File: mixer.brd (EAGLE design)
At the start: 23 x 40 mm, 21 parts, among them U2 SA602AD8-SOIC

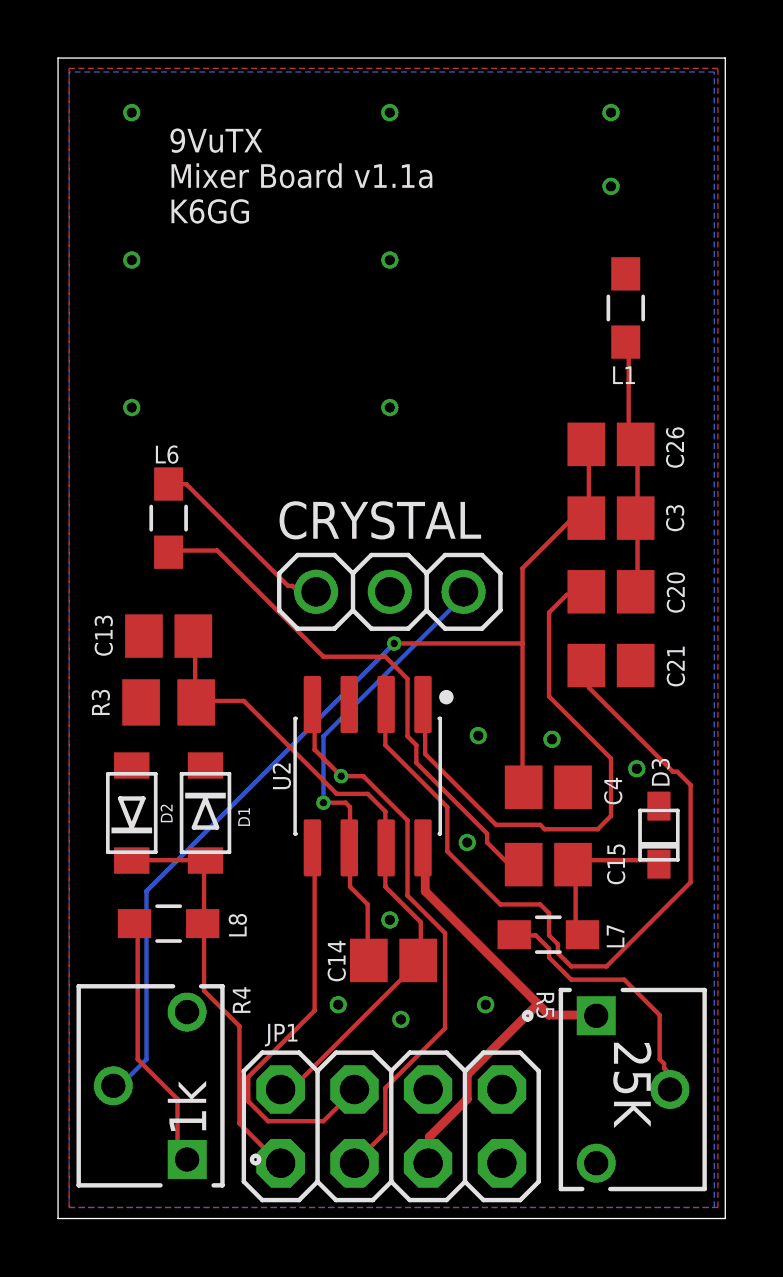
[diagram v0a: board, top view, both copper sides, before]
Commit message: Mixer board 1.1b
* fixed pad size for L7
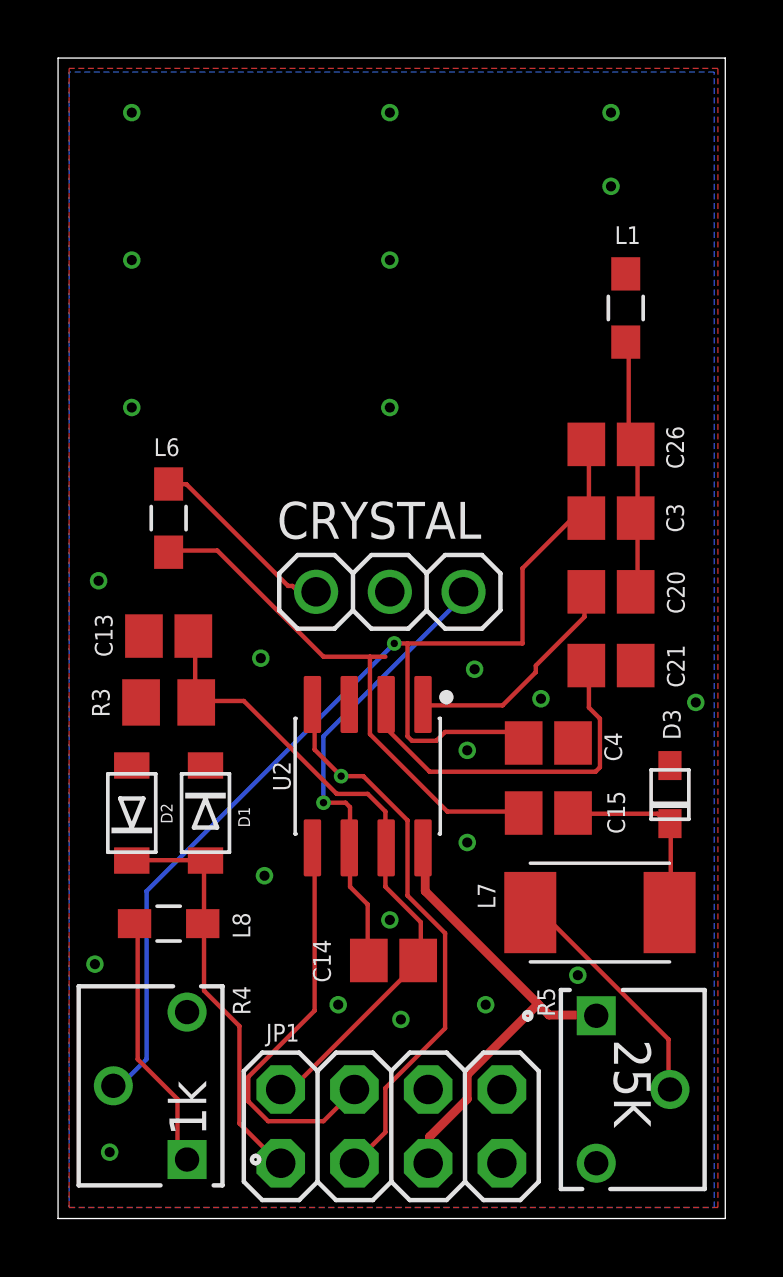
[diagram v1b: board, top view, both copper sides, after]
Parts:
- L7: device MLF2012E5R6KT000:INDC2012X87N -> zort2:INDM4532X32_W
- moved L7 1.93 mm to (18.7, 10.5)
- moved C15 1.78 mm to (16.9, 14.0)
- moved C4 1.52 mm to (16.9, 16.4)
- moved D3 1.45 mm to (21.1, 14.6)
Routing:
- net N$2: track 27.7 -> 13.5 mm
- net N$1: track 18.9 -> 8.04 mm
- net N$5: track 36.9 -> 39.7 mm
- net N$18: track 9.06 -> 8.32 mm
- net N$17: track 6.15 -> 6.75 mm
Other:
- board text added: "9VuTX Mixer Board v1.1b K6GG"
- board text removed: "9VuTX Mixer Board v1.1a K6GG"

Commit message: Some cleanup
* mixer board had incorrect Resistor labels
* updated schematic PNG
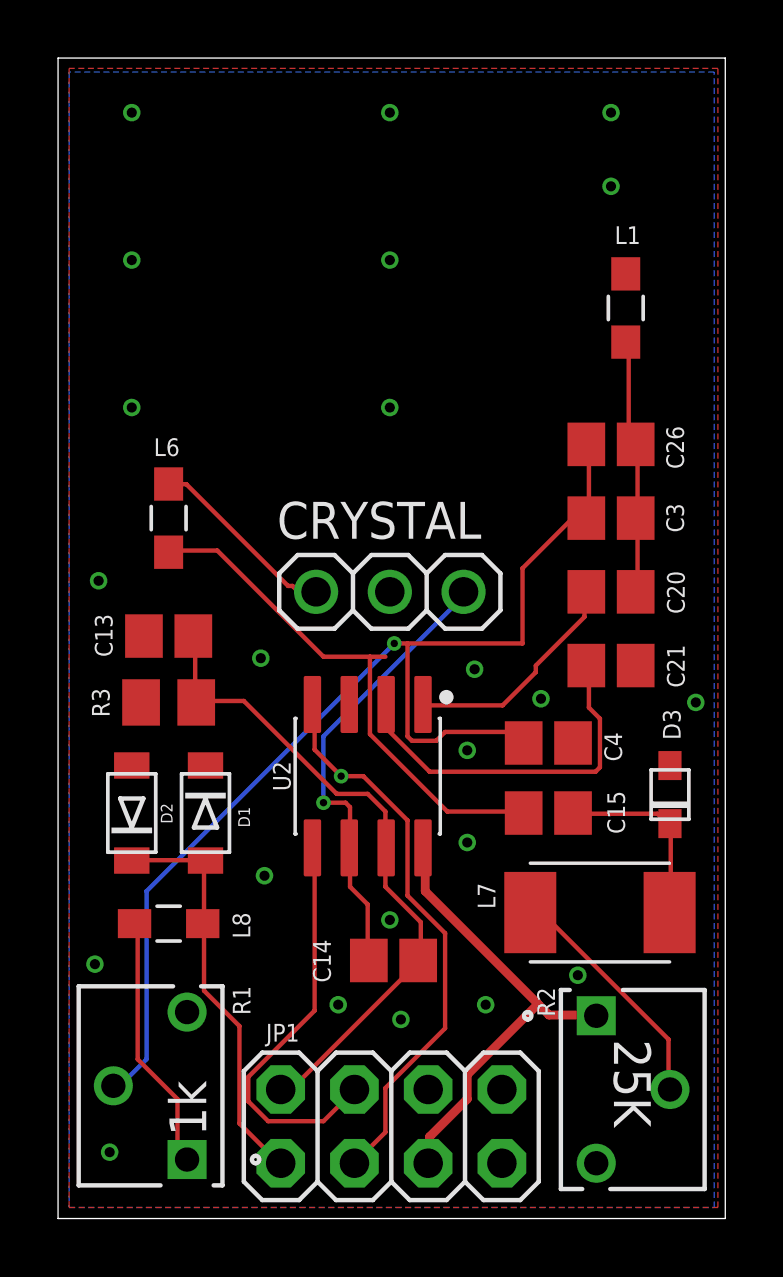
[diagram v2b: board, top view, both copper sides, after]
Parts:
- renumbered R4 to R1, R5 to R2
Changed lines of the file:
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@@
 <?xml version="1.0" encoding="utf-8"?>
 <!DOCTYPE eagle SYSTEM "eagle.dtd">
-<eagle version="9.6.1">
+<eagle version="9.6.2">
 <drawing>
 <settings>
@@
 <attribute name="VALUE" x="7.533" y="15.24" size="1.27" layer="27" rot="R270" align="top-center"/>
 </element>
-<element name="R4" library="zort2" package="POT_3362W" value="1k" x="4.445" y="2.032" smashed="yes" rot="R90">
+<element name="R1" library="zort2" package="POT_3362W" value="1k" x="4.445" y="2.032" smashed="yes" rot="R90">
 <attribute name="BUILT_BY" value="EMA_UL_Team" x="4.445" y="2.032" size="1.778" layer="27" rot="R90" display="off"/>
 <attribute name="MANUFACTURER_PART_NUMBER" value="3362W-1-102LF" x="4.445" y="2.032" size="1.778" layer="27" rot="R90" display="off"/>
@@
 <attribute name="VENDOR" value="Bourns Electronics" x="4.445" y="2.032" size="1.778" layer="27" rot="R90" display="off"/>
 </element>
-<element name="R5" library="zort2" package="POT_3362W" value="25K" x="18.542" y="6.985" smashed="yes" rot="R270">
+<element name="R2" library="zort2" package="POT_3362W" value="25K" x="18.542" y="6.985" smashed="yes" rot="R270">
 <attribute name="BUILT_BY" value="EMA_UL_Team" x="18.542" y="6.985" size="1.778" layer="27" rot="R270" display="off"/>
 <attribute name="MANUFACTURER_PART_NUMBER" value="3362W-1-102LF" x="18.542" y="6.985" size="1.778" layer="27" rot="R270" display="off"/>
@@
 <contactref element="R3" pad="1"/>
 <contactref element="D3" pad="A"/>
-<contactref element="R5" pad="3"/>
-<contactref element="R4" pad="3"/>
+<contactref element="R2" pad="3"/>
+<contactref element="R1" pad="3"/>
 <contactref element="JP1" pad="8"/>
 <polygon width="0.1524" layer="1">
@@
 <signal name="6V_DC" class="1">
 <contactref element="U2" pad="8"/>
-<contactref element="R5" pad="1"/>
+<contactref element="R2" pad="1"/>
 <contactref element="JP1" pad="5"/>
 <wire x1="12.6492" y1="11.2776" x2="12.6492" y2="12.573" width="0.3048" layer="1"/>
@@
 <contactref element="C4" pad="1"/>
 <contactref element="C26" pad="2"/>
-<contactref element="R4" pad="2"/>
+<contactref element="R1" pad="2"/>
 <wire x1="16.002" y1="22.4028" x2="16.002" y2="19.812" width="0.1524" layer="1"/>
 <wire x1="17.6784" y1="24.0792" x2="16.002" y2="22.4028" width="0.1524" layer="1"/>
@@
 <signal name="N$6">
 <contactref element="L8" pad="2"/>
-<contactref element="R4" pad="1"/>
+<contactref element="R1" pad="1"/>
 <wire x1="2.7432" y1="5.4864" x2="2.7432" y2="10.0584" width="0.1524" layer="1"/>
 <wire x1="4.1148" y1="4.1148" x2="2.7432" y2="5.4864" width="0.1524" layer="1"/>
@@
 <signal name="N$18">
 <contactref element="L7" pad="1"/>
-<contactref element="R5" pad="2"/>
+<contactref element="R2" pad="2"/>
 <wire x1="21.0312" y1="6.1722" x2="21.0312" y2="4.4958" width="0.1524" layer="1"/>
 <wire x1="16.6878" y1="10.5156" x2="21.0312" y2="6.1722" width="0.1524" layer="1"/>

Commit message: v1.2 boards
* corrected C22 as a 33uF (vs 33pF) capacitor with a 1206 footprint
* Q2 emitter is now tied to Q1 emitter and KEY_IN to cut down on self resonance
* Unused pin 4 on JP1 now tied to GND
* All pins on JP1 labelled on top and bottom of each board
* lots more GND vias
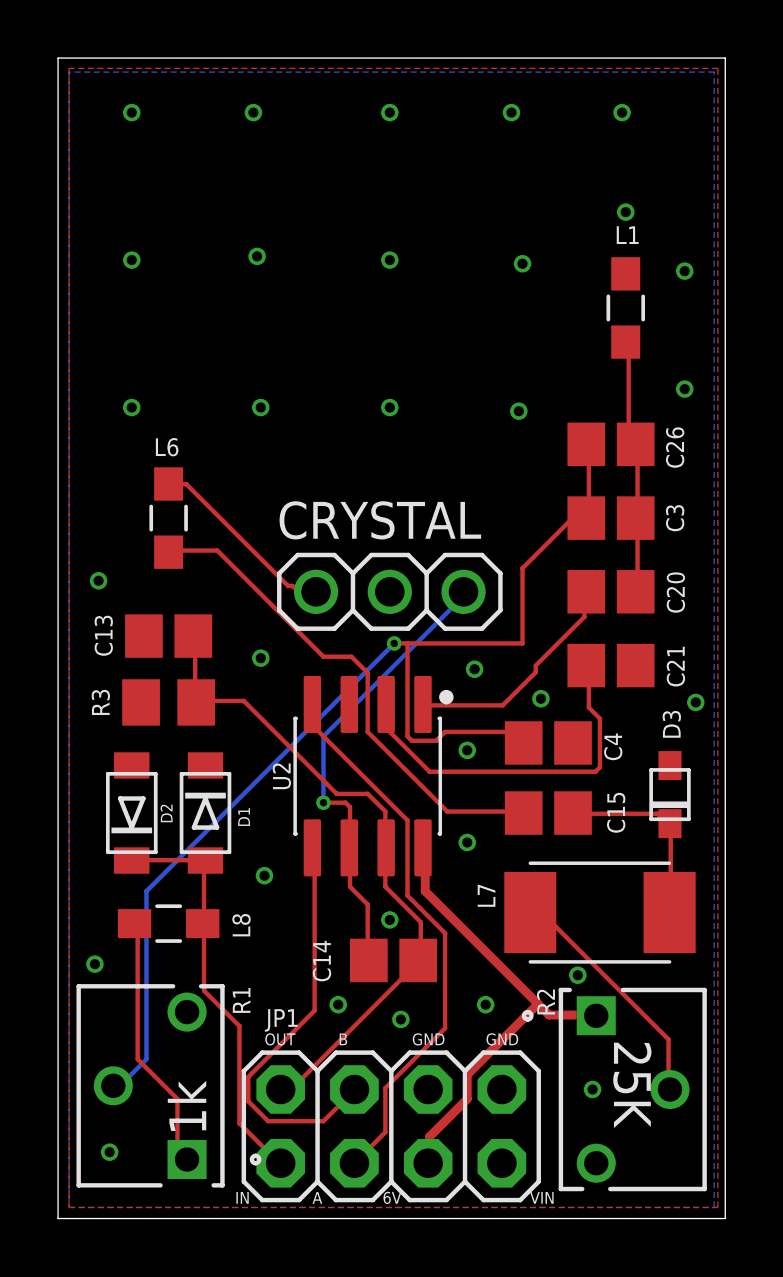
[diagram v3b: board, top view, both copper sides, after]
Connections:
- net GND: now also JP1.6
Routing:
- net N$16: track 18.1 -> 17.2 mm
- net OUT_A: track 19.5 -> 19.0 mm, vias 1 -> 0
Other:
- board text added: "6V"
- board text added: "9VμTX Mixer Board v1.2 K6GG & K6JCA"
- board text added: "A"
- board text added: "ATTN"
- board text added: "B"
- board text added: "GND"
- board text added: "IN"
- board text added: "OUT"
- board text added: "VIN"
- board text added: "VXO"
- board text removed: "9VuTX Mixer Board v1.1b K6GG"
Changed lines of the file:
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@@
 <wire x1="22.987" y1="39.9796" x2="0" y2="39.9796" width="0" layer="20"/>
 <wire x1="0" y1="39.9796" x2="0" y2="0" width="0" layer="20"/>
-<text x="17.78" y="34.29" size="0.8128" layer="26" rot="MR0">9VuTX
-Mixer Board v1.1b
-K6GG</text>
+<text x="17.78" y="34.29" size="0.8128" layer="26" rot="MR0">9VμTX
+Mixer Board v1.2
+K6GG &amp; K6JCA</text>
+<text x="6.096" y="0.508" size="0.4064" layer="25">IN</text>
+<text x="7.112" y="5.969" size="0.4064" layer="25">OUT</text>
+<text x="9.652" y="5.969" size="0.4064" layer="25">B</text>
+<text x="8.763" y="0.508" size="0.4064" layer="25">A</text>
+<text x="12.192" y="5.969" size="0.4064" layer="25">GND</text>
+<text x="14.732" y="5.969" size="0.4064" layer="25">GND</text>
+<text x="11.176" y="0.508" size="0.4064" layer="25">6V</text>
+<text x="16.256" y="0.508" size="0.4064" layer="25">VIN</text>
+<text x="15.875" y="0.381" size="0.4064" layer="26" rot="MR0">VIN</text>
+<text x="13.081" y="0.381" size="0.4064" layer="26" rot="MR0">6V</text>
+<text x="10.414" y="0.381" size="0.4064" layer="26" rot="MR0">A</text>
+<text x="8.001" y="0.381" size="0.4064" layer="26" rot="MR0">IN</text>
+<text x="8.255" y="5.588" size="0.4064" layer="26" rot="MR0">OUT</text>
+<text x="10.414" y="5.715" size="0.4064" layer="26" rot="MR0">B</text>
+<text x="13.335" y="5.588" size="0.4064" layer="26" rot="MR0">GND</text>
+<text x="15.875" y="5.588" size="0.4064" layer="26" rot="MR0">GND</text>
+<text x="22.225" y="1.143" size="0.8128" layer="26" rot="MR0">VXO</text>
+<text x="3.556" y="1.143" size="0.8128" layer="26" rot="MR0">ATTN</text>
 </plain>
 <attributes>
@@
 </element>
 <element name="JP1" library="adafruit" library_urn="urn:adsk.eagle:library:420" package="2X04" package3d_urn="urn:adsk.eagle:package:6240893/1" value="" x="11.4808" y="3.175" smashed="yes">
-<attribute name="NAME" x="7.1628" y="6.096" size="0.6096" layer="25" ratio="10"/>
+<attribute name="NAME" x="7.1628" y="6.604" size="0.6096" layer="25" ratio="10"/>
 <attribute name="VALUE" x="6.4008" y="-1.27" size="1.27" layer="27"/>
 </element>
@@
 <via x="11.43" y="33.02" extent="1-16" drill="0.35"/>
 <via x="11.43" y="27.94" extent="1-16" drill="0.35"/>
-<via x="19.05" y="38.1" extent="1-16" drill="0.35"/>
-<via x="19.05" y="35.56" extent="1-16" drill="0.35"/>
+<via x="19.431" y="38.1" extent="1-16" drill="0.35"/>
+<via x="19.558" y="34.671" extent="1-16" drill="0.35"/>
 <via x="14.351" y="18.923" extent="1-16" drill="0.35"/>
 <via x="16.637" y="17.907" extent="1-16" drill="0.35"/>
@@
 <via x="1.27" y="8.763" extent="1-16" drill="0.35"/>
 <via x="1.778" y="2.286" extent="1-16" drill="0.35"/>
+<contactref element="JP1" pad="6"/>
+<via x="18.415" y="4.445" extent="1-16" drill="0.35"/>
+<via x="6.858" y="33.147" extent="1-16" drill="0.35"/>
+<via x="6.731" y="38.1" extent="1-16" drill="0.35"/>
+<via x="6.985" y="27.94" extent="1-16" drill="0.35"/>
+<via x="16.002" y="32.893" extent="1-16" drill="0.35"/>
+<via x="15.875" y="27.813" extent="1-16" drill="0.35"/>
+<via x="15.621" y="38.1" extent="1-16" drill="0.35"/>
+<via x="21.59" y="28.575" extent="1-16" drill="0.35"/>
+<via x="21.59" y="32.639" extent="1-16" drill="0.35"/>
 </signal>
 <signal name="6V_DC" class="1">
@@
 <contactref element="U2" pad="4"/>
 <contactref element="JP1" pad="3"/>
-<wire x1="8.8392" y1="16.1544" x2="8.8392" y2="17.6784" width="0.1524" layer="1"/>
-<wire x1="9.7536" y1="15.24" x2="8.8392" y2="16.1544" width="0.1524" layer="1"/>
 <wire x1="8.8392" y1="17.6784" x2="8.763" y2="17.7101" width="0.1524" layer="1"/>
-<via x="9.7536" y="15.24" extent="1-16" drill="0.254"/>
-<wire x1="10.5156" y1="15.24" x2="9.7536" y2="15.24" width="0.1524" layer="1"/>
-<wire x1="12.0396" y1="13.716" x2="10.5156" y2="15.24" width="0.1524" layer="1"/>
 <wire x1="12.0396" y1="11.1252" x2="12.0396" y2="13.716" width="0.1524" layer="1"/>
 <wire x1="13.335" y1="9.8298" x2="12.0396" y2="11.1252" width="0.1524" layer="1"/>
@@
 <wire x1="11.2776" y1="2.9718" x2="11.2776" y2="4.4958" width="0.1524" layer="1"/>
 <wire x1="10.2108" y1="1.905" x2="11.2776" y2="2.9718" width="0.1524" layer="1"/>
+<wire x1="8.8392" y1="16.9164" x2="8.8392" y2="17.6784" width="0.1524" layer="1"/>
+<wire x1="12.0396" y1="13.716" x2="8.8392" y2="16.9164" width="0.1524" layer="1"/>
 </signal>
 <signal name="OUT_B">
@@
 <wire x1="5.4864" y1="23.0124" x2="3.81" y2="23.0124" width="0.1524" layer="1"/>
 <wire x1="9.144" y1="19.3548" x2="5.4864" y2="23.0124" width="0.1524" layer="1"/>
-<wire x1="11.2776" y1="19.3548" x2="10.7442" y2="19.3548" width="0.1524" layer="1"/>
-<wire x1="10.7442" y1="19.3548" x2="9.144" y2="19.3548" width="0.1524" layer="1"/>
 <wire x1="3.81" y1="23.0124" x2="3.81" y2="22.955" width="0.1524" layer="1"/>
-<wire x1="13.4112" y1="14.0208" x2="16.002" y2="14.0208" width="0.1524" layer="1"/>
-<wire x1="10.7442" y1="16.6878" x2="13.4112" y2="14.0208" width="0.1524" layer="1"/>
-<wire x1="10.7442" y1="19.3548" x2="10.7442" y2="16.6878" width="0.1524" layer="1"/>
+<wire x1="16.002" y1="14.0208" x2="13.4112" y2="14.0208" width="0.1524" layer="1"/>
 <wire x1="16.002" y1="14.0208" x2="16.041" y2="13.97" width="0.1524" layer="1"/>
+<wire x1="10.668" y1="16.764" x2="10.668" y2="18.796" width="0.1524" layer="1"/>
+<wire x1="10.1092" y1="19.3548" x2="9.144" y2="19.3548" width="0.1524" layer="1"/>
+<wire x1="13.4112" y1="14.0208" x2="10.668" y2="16.764" width="0.1524" layer="1"/>
+<wire x1="10.668" y1="18.796" x2="10.1092" y2="19.3548" width="0.1524" layer="1"/>
 </signal>
 <signal name="N$17">

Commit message: v1.2 updated inductors
* updated L3 to a 650mA capable 5.6uH flat package
* updated L4 to a 3A capable 15uH flat package... 16uH are difficult to come by
* general board cleanup for readability
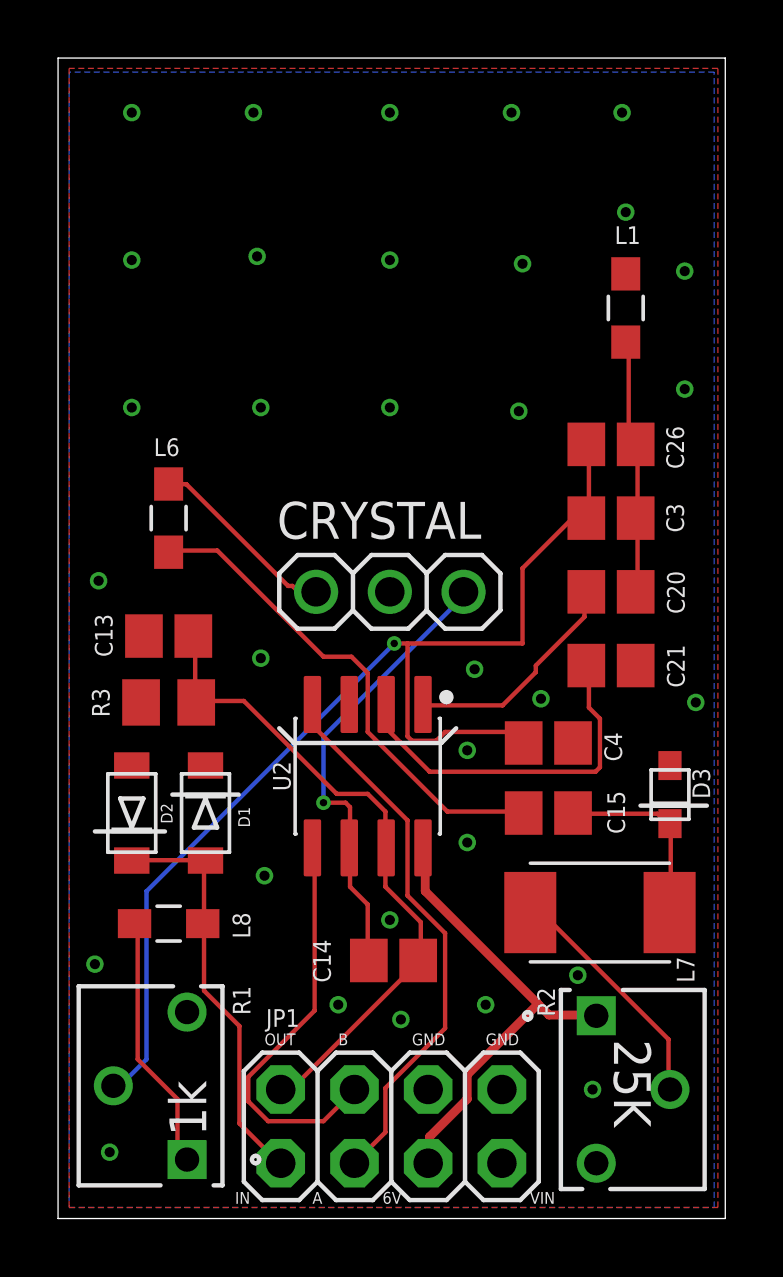
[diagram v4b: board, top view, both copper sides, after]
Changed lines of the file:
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@@
 <text x="22.225" y="1.143" size="0.8128" layer="26" rot="MR0">VXO</text>
 <text x="3.556" y="1.143" size="0.8128" layer="26" rot="MR0">ATTN</text>
+<wire x1="7.62" y1="16.891" x2="8.128" y2="16.383" width="0.1524" layer="21"/>
+<wire x1="8.128" y1="16.383" x2="13.208" y2="16.383" width="0.1524" layer="21"/>
+<wire x1="13.208" y1="16.383" x2="13.716" y2="16.891" width="0.1524" layer="21"/>
+<wire x1="1.27" y1="13.335" x2="3.683" y2="13.335" width="0.1524" layer="21"/>
+<wire x1="3.937" y1="14.605" x2="6.223" y2="14.605" width="0.1524" layer="21"/>
+<wire x1="20.066" y1="14.224" x2="22.352" y2="14.224" width="0.1524" layer="21"/>
 </plain>
 <attributes>
@@
 </element>
 <element name="D3" library="adafruit" library_urn="urn:adsk.eagle:library:420" package="SOD-323F" package3d_urn="urn:adsk.eagle:package:6240873/1" value="MV2102" x="21.082" y="14.605" smashed="yes" rot="R270">
-<attribute name="NAME" x="20.839" y="17.548" size="0.6096" layer="25" font="vector" rot="R270"/>
+<attribute name="NAME" x="21.855" y="15.516" size="0.6096" layer="25" font="vector" rot="R270"/>
 <attribute name="VALUE" x="19.382" y="16.705" size="0.8128" layer="27" font="vector" rot="R270"/>
 </element>
@@
 </element>
 <element name="L7" library="zort2" package="INDM4532X32_W" value="560uH" x="18.669" y="10.541" smashed="yes">
-<attribute name="NAME" x="15.067" y="10.665" size="0.6096" layer="25" rot="R90"/>
+<attribute name="NAME" x="21.925" y="8.125" size="0.6096" layer="25" rot="R90"/>
 <attribute name="VALUE" x="16.634" y="9.136" size="0.5" layer="27"/>
 </element>
